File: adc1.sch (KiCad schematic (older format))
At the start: 31 parts, among them U1 AD7960BCPZ-RL7, U3 ADA4932-1YCPZ-R7, X1 BU-SMA-G, X2 BU-SMA-G

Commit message: cleanup from Eagle import
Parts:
- C11, C12, C13, C14, C15, C16, C17, C18, C19, C20, C27, C4, C5, C54: footprint adc_dac_v1:C0603 -> Capacitor_SMD:C_0603_1608Metric; symbol adc_dac_v1-eagle-import:C-USC0603 -> Device:C
- R10, R11, R12, R13, R15, R16, R17, R18, R19, R20, R8, R9: footprint adc_dac_v1:R0603 -> Resistor_SMD:R_0603_1608Metric; symbol adc_dac_v1-eagle-import:R-US_R0603 -> Device:R_US
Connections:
- net labels added: +1V8, +5V
- net labels removed: 1V8, 5V, N$11, N$12, N$13, N$14, N$15, N$16, N$17, N$18
- wire segments 159 -> 175

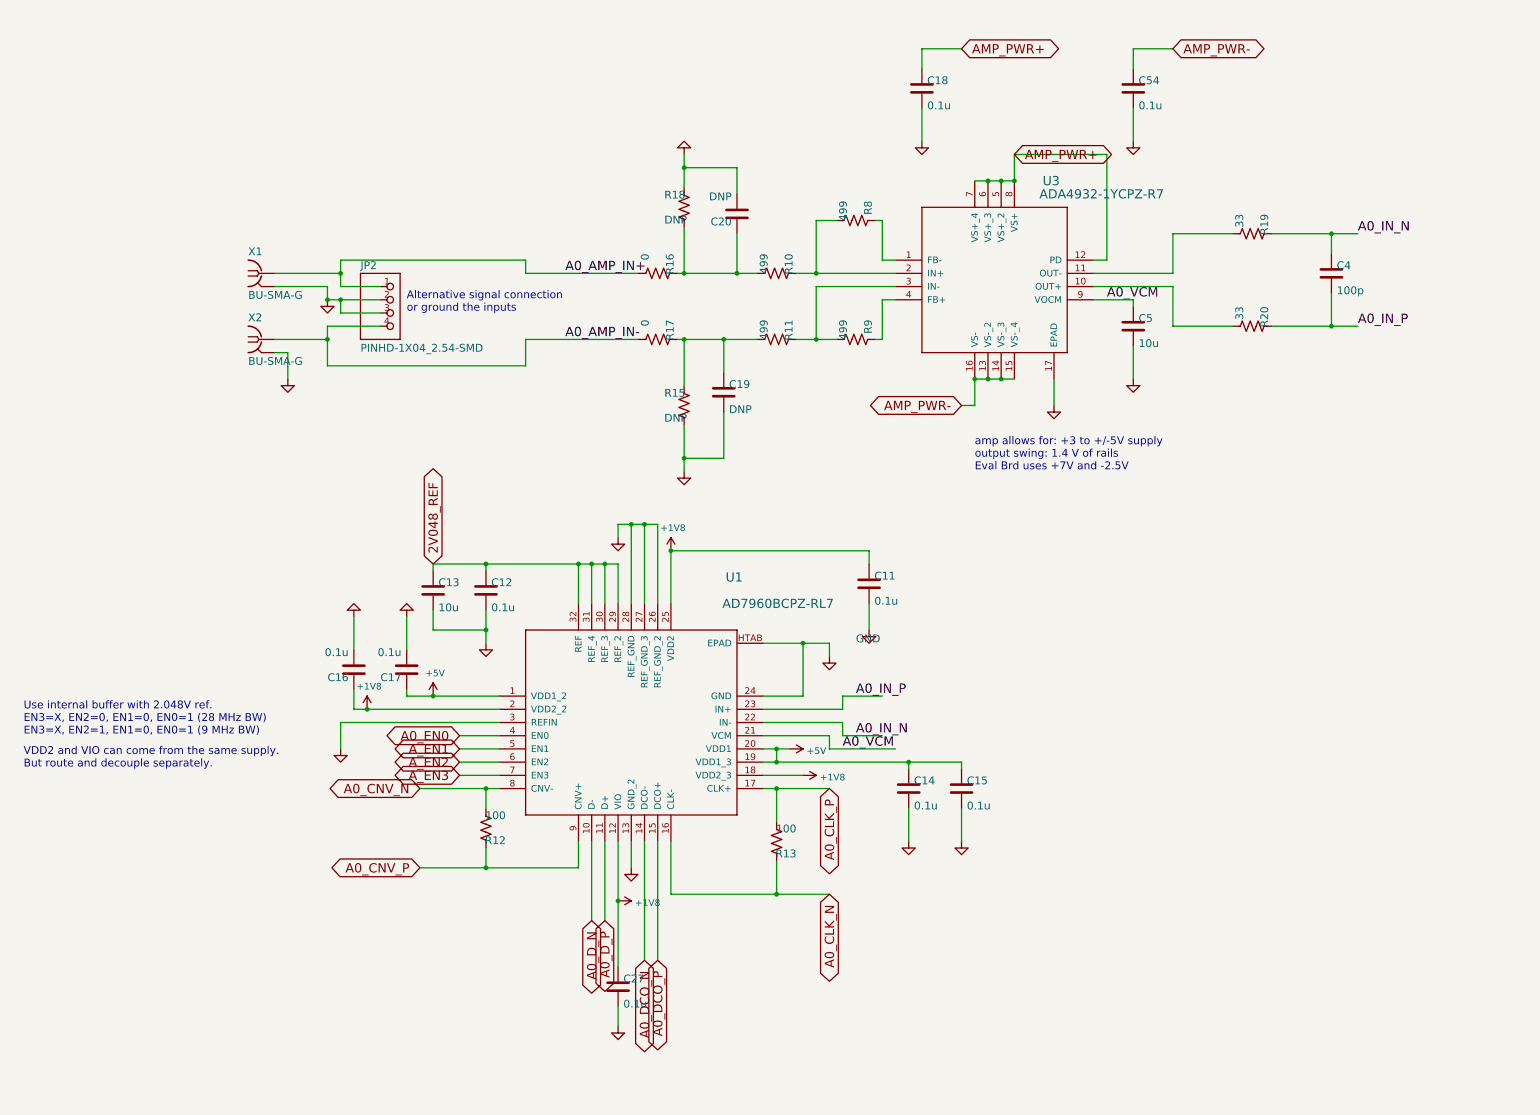
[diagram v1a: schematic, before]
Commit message: updates to fast adc schematic
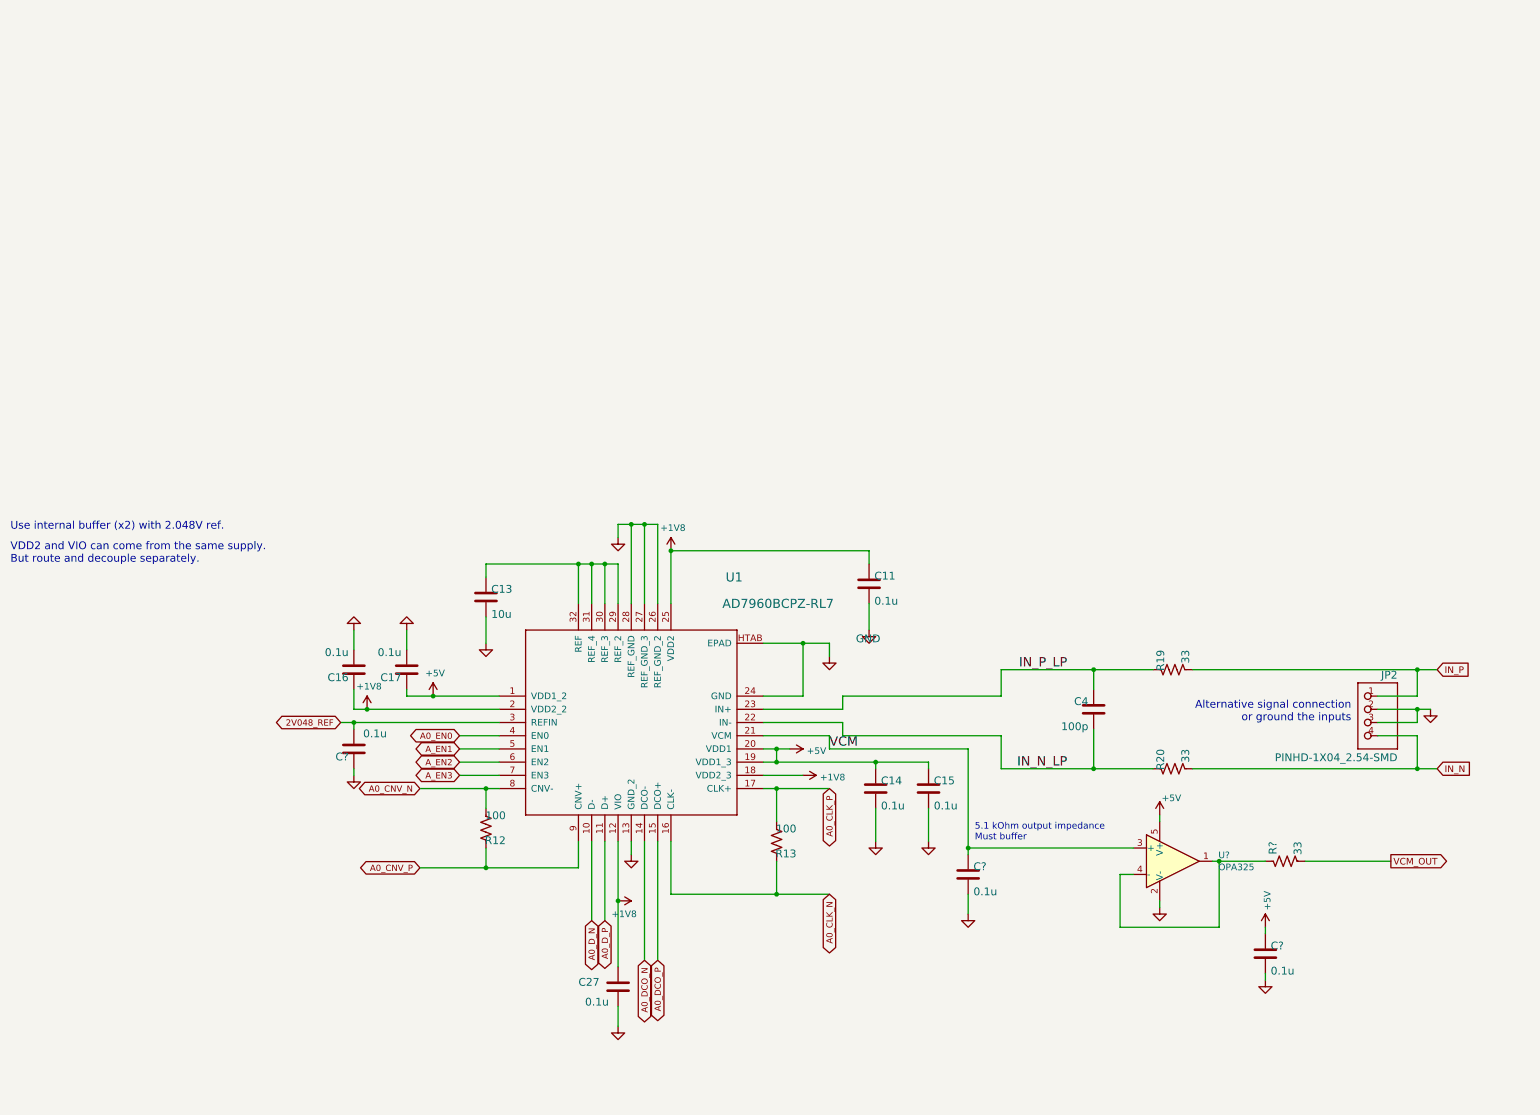
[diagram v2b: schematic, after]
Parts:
- removed C12, C18, C54: 0.1u, Capacitor_SMD:C_0603_1608Metric, symbol Device:C
- removed C19, C20: DNP, Capacitor_SMD:C_0603_1608Metric, symbol Device:C
- removed C5: 10u, Capacitor_SMD:C_0603_1608Metric, symbol Device:C
- removed R10, R11, R8, R9: 499, Resistor_SMD:R_0603_1608Metric, symbol Device:R_US
- removed R15, R18: DNP, Resistor_SMD:R_0603_1608Metric, symbol Device:R_US
- removed R16, R17: 0, Resistor_SMD:R_0603_1608Metric, symbol Device:R_US
- removed U3: ADA4932-1YCPZ-R7, adc_dac_v1:CP_16_2, symbol adc_dac_v1-eagle-import:ADA4932-1YCPZ-R7
- removed X1, X2: BU-SMA-G, adc_dac_v1:BU-SMA-G, symbol adc_dac_v1-eagle-import:BU-SMA-G
- added C? (x3): 0.1u, Capacitor_SMD:C_0603_1608Metric, symbol Device:C
- added R?: 33, Resistor_SMD:R_0603_1608Metric, symbol Device:R_US
- added U?: OPA325, Package_TO_SOT_SMD:SOT-23-5, symbol covg-kicad:OPA325
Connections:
- net A0_AMP_IN+ is gone; now on net IN_P: JP2.1
- net A0_AMP_IN- is gone; now on net IN_N: JP2.4
- net +5V: now also C?.1, U?.5 (V+)
- net 2V048_REF: now also U1.3 (REFIN), C?.2; no longer C13.1, U1.29 (REF_2), U1.30 (REF_3), U1.31 (REF_4), U1.32 (REF)
- net GND: now also C?.1, C?.2, C?.2, U?.2 (V-); no longer U1.3 (REFIN)
- net IN_N: now reaches R20.2
- net IN_P: now reaches R19.2
- net A0_IN_N renamed IN_P_LP
- net IN_P_LP: now also U1.23 (IN+); no longer U1.22 (IN-)
- net A0_IN_P renamed IN_N_LP
- net IN_N_LP: now also U1.22 (IN-); no longer U1.23 (IN+)
- net A0_VCM renamed VCM
- net VCM: now also C?.1, U?.3 (+)
- new net: C13.1, U1.29 (REF_2), U1.30 (REF_3), U1.31 (REF_4), U1.32 (REF)
- new net: R?.1, U?.1, U?.4 (-)
- new net VCM_OUT: R?.2
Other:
- note added: "5.1 kOhm output impedance\nMust buffer\n"
- note added: "Use internal buffer (x2) with 2.048V ref. \n “External reference of 2.048 V applied to the REFIN pin\n(high impedance input). The on-chip buffer gains this by 2\nand drives the REF pin with 4.096 V” \nEN3=X, EN2=0, EN1=0, EN0=1 (28 MHz BW)\nEN3=X, EN2=1, EN1=0, EN0=1 (9 MHz BW)"
- note removed: "Use internal buffer with 2.048V ref. \nEN3=X, EN2=0, EN1=0, EN0=1 (28 MHz BW)\nEN3=X, EN2=1, EN1=0, EN0=1 (9 MHz BW)"
- note removed: "amp allows for: +3 to +/-5V supply\noutput swing: 1.4 V of rails\nEval Brd uses +7V and -2.5V"
- moved on the sheet: C13, C14, C15, C4, JP2, R19, R20
